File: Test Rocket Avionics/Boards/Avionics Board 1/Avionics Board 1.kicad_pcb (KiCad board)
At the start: 4 copper layers, 50 x 50 mm, 71 parts, among them J1 USB_A, J14 1S LiPo, J2 1S LiPo, J3 EXPANSION_HEADER, J4 USB_A, J5 SERVO, M2.5 CHASSIS_GND, U1 ECS-.327-12.5-17X-TR, U10 NC7WZ07, U11 LMR62014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

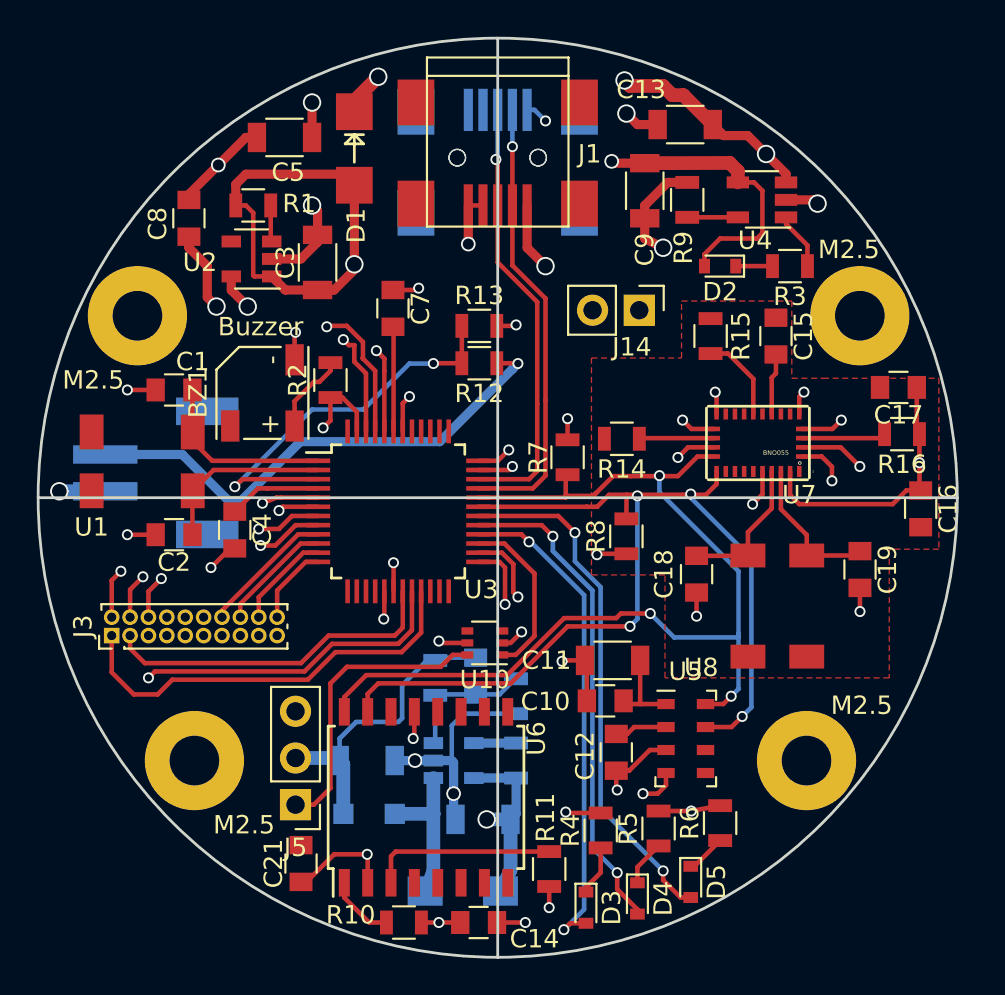
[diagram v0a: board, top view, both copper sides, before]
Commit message: Remove DS3231 and expand the J3 connector to include USB and improve pin ordering. Various bug fixes
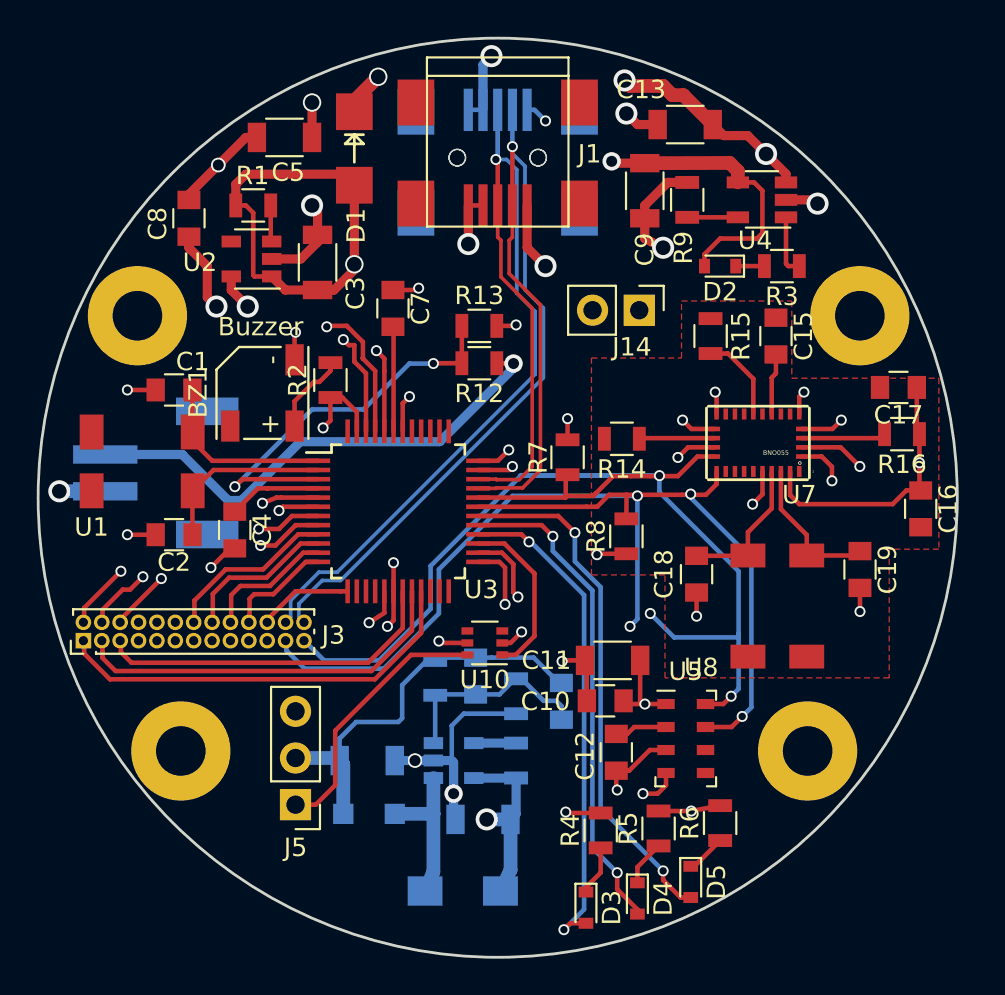
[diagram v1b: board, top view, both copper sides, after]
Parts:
- removed C21: 1u, Capacitors_SMD:C_0805
- removed M2.5: CHASSIS_GND, Mounting_Holes:MountingHole_2.7mm_M2.5_Pad
- removed R10, R11: 10k, Resistors_SMD:R_0805
- removed U6: DS3231-SO16, Housings_SOIC:SOIC-16W_7.5x10.3mm_Pitch1.27mm
- added J13: CHASSIS_GND, Mounting_Holes:MountingHole_2.7mm_M2.5_Pad, F.Cu at (28.0, 117.0)
- C22: renamed from C14; moved to B.Cu
- J3: footprint Pin_Headers:Pin_Header_Straight_2x10_Pitch1.00mm -> Pin_Headers:Pin_Header_Straight_2x13_Pitch1.00mm
- moved C22 12.8 mm to (48.7, 114.3), turned to 90 degrees
- moved G*** 1.92 mm to (44.9, 102.0)
- moved J3 1.56 mm to (22.7, 111.0)
- moved G*** 0.72 mm to (40.1, 105.0)
- moved J11 0.53 mm to (62.1, 117.0)
- moved R3 0.44 mm to (60.7, 90.6)
- renumbered M2.5 to J10, M2.5 to J11, M2.5 to J12
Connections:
- C22 pad 1: Net-(C14-Pad1) -> Net-(C22-Pad1)
- J3 pad 11: /D11 -> +3V3
- J3 pad 19: +3V3 -> /D13
- J3 pad 3: /MOSI -> /SCK
- J3 pad 5: /SCK -> /MOSI
- J3 pad 9: /D13 -> +3V3
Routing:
- net /USB_D-: track 24.6 -> 57.0 mm
- net /USB_D+: track 24.0 -> 56.1 mm
- net +3V3: track 75.0 -> 90.9 mm, vias 16 -> 14
- net /SCL: track 55.7 -> 68.8 mm
- net Net-(R11-Pad1): track 10.2 -> 0.00 mm
- net /SDA: track 55.6 -> 64.2 mm
- net GND: track 110.0 -> 117.3 mm, vias 35 -> 36
- net /D4: track 0.00 -> 5.06 mm
- net /6V_SERVO_SUPPLY: track 18.1 -> 22.1 mm
- net /D13: track 26.1 -> 22.1 mm
- net /D11: track 22.6 -> 18.7 mm
- net Net-(C22-Pad1): track 7.41 -> 11.2 mm
- net Net-(R10-Pad1): track 3.66 -> 0.00 mm
- net /A3: track 7.31 -> 9.33 mm
- net /A4: track 6.32 -> 8.33 mm
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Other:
- outline, holes or cut-outs redrawn

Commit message: Add micro SD Card, clean up ref des, power 6v boost directly from battery instead of 3.3V rail
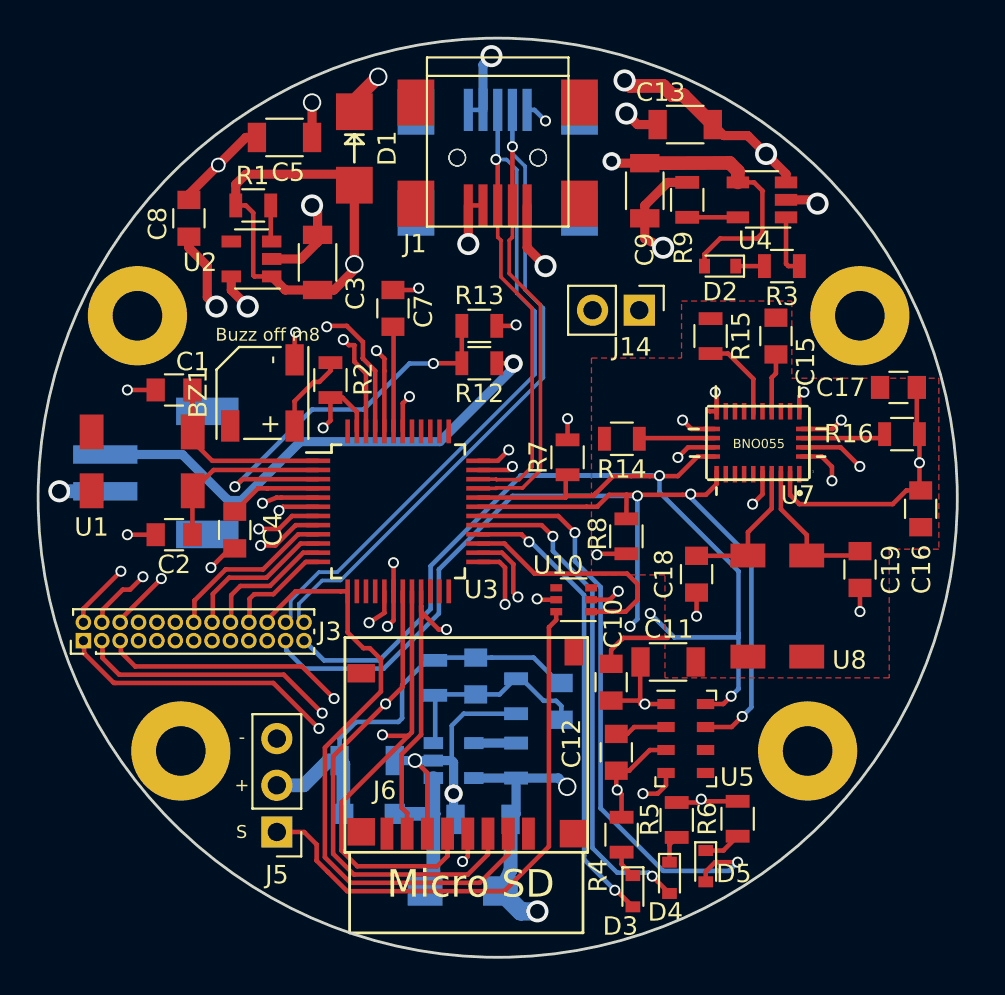
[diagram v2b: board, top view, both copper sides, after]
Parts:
- added J6: Micro_SD_Card, DannysLib:MicroSD_DM3D-SF, F.Cu at (39.2, 121.5)
- BZ1: value Buzzer -> Buzz off m8
- moved U10 5.37 mm to (49.4, 108.8)
- moved C11 3.02 mm to (54.5, 112.2), turned to 0 degrees
- moved D3 2.71 mm to (52.6, 124.6)
- moved D4 2.07 mm to (54.6, 123.9)
- moved J5 1.80 mm to (33.2, 121.4)
- moved D5 1.18 mm to (56.6, 123.3)
- moved R4 1.16 mm to (52.0, 121.6)
- moved R5 1.09 mm to (55.0, 120.8)
- moved C10 1.06 mm to (51.4, 113.3), turned to 90 degrees
- moved R6 0.98 mm to (58.3, 120.7)
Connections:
- C20 pad 1: +3V3 -> +BATT
- L1 pad 2: +3V3 -> +BATT
- R17 pad 1: +3V3 -> +BATT
- U11 pad 5: +3V3 -> +BATT
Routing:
- net +BATT: track 75.5 -> 117.5 mm, vias 4 -> 6
- net /D4: track 5.06 -> 34.1 mm
- net /MOSI: track 19.0 -> 42.6 mm, vias 0 -> 2
- net /SCK: track 21.1 -> 42.6 mm, vias 0 -> 2
- net /MISO: track 22.9 -> 40.1 mm, vias 0 -> 2
- net Net-(J5-Pad1): track 14.7 -> 30.7 mm
- net +3V3: track 90.9 -> 82.9 mm
- net GND: track 117.3 -> 122.8 mm, vias 36 -> 34
- net /D7: track 28.4 -> 32.8 mm
- net /D10: track 9.32 -> 13.2 mm
- net /D12: track 27.1 -> 25.2 mm
- net /6V_SERVO_SUPPLY: track 22.1 -> 23.9 mm
- net Net-(D4-Pad1): track 2.84 -> 1.51 mm
- net Net-(D3-Pad1): track 2.73 -> 1.53 mm
- net /D6: track 26.8 -> 27.4 mm
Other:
- board text added: "+"
- board text added: "-"
- board text added: "S"

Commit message: Add LMS303C and BMP280
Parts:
- removed C18, C19: 22p, Capacitors_SMD:C_0805
- added C14: 100n, Capacitors_SMD:C_0805, F.Cu at (60.4, 111.2)
- added C23: 100n, Capacitors_SMD:C_0805, F.Cu at (65.2, 106.1)
- added C24: 10u, Capacitors_SMD:C_1206, F.Cu at (65.2, 110.9)
- added U6: LSM303C, Housings_LGA:LGA-12_2x2mm_Pitch0.5mm, F.Cu at (61.7, 108.0)
- BZ1: value Buzz off m8 -> Buzzer
- U8: value ECS-.327-12.5-17X-TR -> BMP280; footprint DannysLib:XC1195CT-ND -> DannysLib:BMP280
- moved U8 3.30 mm to (55.6, 105.9), turned to 0 degrees
- moved L1 0.47 mm to (43.8, 124.8)
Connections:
- U8 pad 1: /BNO_OSC_OUT -> GND
- U8 pad 2: (no net) -> +3V3
- U8 pad 3: (no net) -> /SDA
- U8 pad 4: /BNO_OSC_IN -> /SCL
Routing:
- net GND: track 122.8 -> 145.0 mm, vias 34 -> 38
- net /SCL: track 68.8 -> 80.3 mm, vias 3 -> 4
- net +3V3: track 82.9 -> 94.0 mm, vias 14 -> 18
- net /BNO_OSC_IN: track 8.15 -> 0.00 mm
- net /BNO_OSC_OUT: track 7.91 -> 0.00 mm
- net /SDA: track 64.2 -> 69.6 mm, vias 4 -> 5
- net Net-(C14-Pad1): track 0.00 -> 2.46 mm

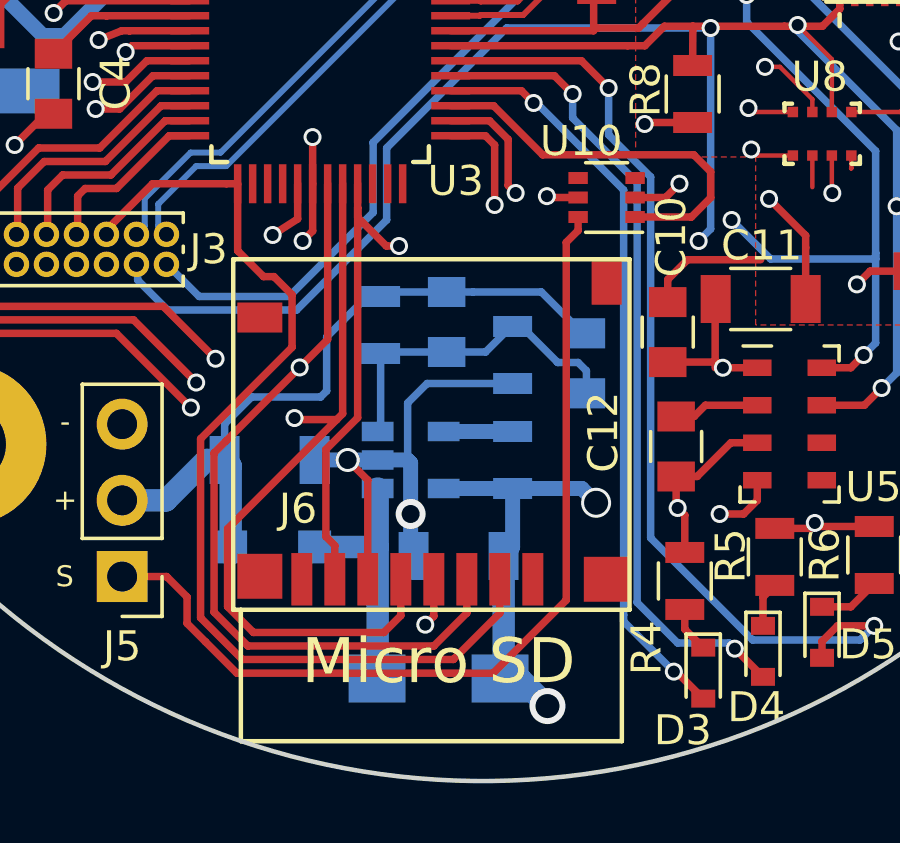
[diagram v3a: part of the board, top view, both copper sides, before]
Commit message: Create Gerbers, move SD card up for more error margin
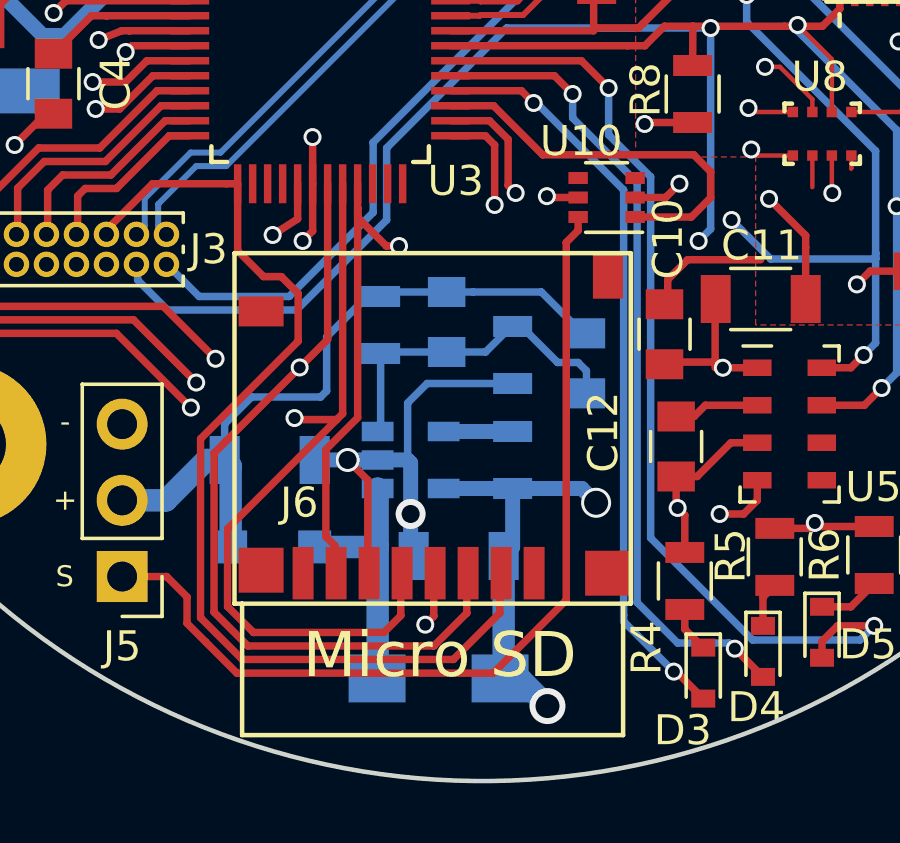
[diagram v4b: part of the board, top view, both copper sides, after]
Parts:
- moved J6 0.21 mm to (39.3, 121.3)
- moved C10 0.13 mm to (51.3, 113.3)
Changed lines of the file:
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@@
   )
   (module Capacitors_SMD:C_0805 (layer F.Cu)
-    (at 51.4096 113.2586 90)
+    (at 51.30292 113.32972 90)
     (descr "Capacitor SMD 0805, reflow soldering, AVX (see smccp.pdf)")
     (tags "capacitor 0805")
@@
   )
   (module DannysLib:MicroSD_DM3D-SF (layer F.Cu)
-    (at 39.21252 121.49836)
+    (at 39.2548 121.29516)
     (fp_text reference J6 (at -0.127 -2.3495) (layer F.SilkS)
       (effects (font (size 1 1) (thickness 0.15)))
@@
   (segment (start 32.74 109.811998) (end 34.237998 108.314) (width 0.25) (layer F.Cu) (net 36))
   (segment (start 32.74 109.922) (end 32.74 109.811998) (width 0.25) (layer F.Cu) (net 36))
-  (segment (start 45.81252 122.62336) (end 45.81252 121.49836) (width 0.25) (layer F.Cu) (net 36))
-  (segment (start 37.227637 124.171299) (end 44.26458 124.1713) (width 0.25) (layer F.Cu) (net 36))
-  (segment (start 35.837501 122.781161) (end 37.227637 124.171299) (width 0.25) (layer F.Cu) (net 36))
-  (segment (start 35.8375 116.816058) (end 35.837501 122.781161) (width 0.25) (layer F.Cu) (net 36))
-  (segment (start 37.074 108.314) (end 37.074 110.54604) (width 0.25) (layer F.Cu) (net 36))
-  (segment (start 37.074 110.54604) (end 37.93744 111.40948) (width 0.25) (layer F.Cu) (net 36))
-  (segment (start 44.26458 124.1713) (end 45.81252 122.62336) (width 0.25) (layer F.Cu) (net 36))
-  (segment (start 38.283642 111.40948) (end 38.887521 112.013359) (width 0.25) (layer F.Cu) (net 36))
-  (segment (start 37.93744 111.40948) (end 38.283642 111.40948) (width 0.25) (layer F.Cu) (net 36))
-  (segment (start 38.887521 112.013359) (end 38.887521 113.766037) (width 0.25) (layer F.Cu) (net 36))
-  (segment (start 38.887521 113.766037) (end 35.8375 116.816058) (width 0.25) (layer F.Cu) (net 36))
   (segment (start 36.14 97.772) (end 36.14 99.022) (width 0.25) (layer F.Cu) (net 37))
   (via (at 26.94 107.622) (size 0.6) (drill 0.4) (layers F.Cu B.Cu) (net 37))
@@
   (segment (start 63.12408 108.82376) (end 63.12408 112.37976) (width 0.25) (layer F.Cu) (net 2))
   (segment (start 63.4238 108.52404) (end 63.12408 108.82376) (width 0.25) (layer F.Cu) (net 2))
+  (segment (start 38.529122 111.40948) (end 37.93744 111.40948) (width 0.25) (layer F.Cu) (net 36))
+  (segment (start 39.0906 113.562958) (end 39.0906 111.970958) (width 0.25) (layer F.Cu) (net 36))
+  (segment (start 37.074 110.54604) (end 37.074 108.314) (width 0.25) (layer F.Cu) (net 36))
+  (segment (start 45.81252 121.49836) (end 45.81252 122.62336) (width 0.25) (layer F.Cu) (net 36))
+  (segment (start 45.81252 122.62336) (end 44.26458 124.1713) (width 0.25) (layer F.Cu) (net 36))
+  (segment (start 37.93744 111.40948) (end 37.074 110.54604) (width 0.25) (layer F.Cu) (net 36))
+  (segment (start 44.26458 124.1713) (end 37.227637 124.171299) (width 0.25) (layer F.Cu) (net 36))
+  (segment (start 37.227637 124.171299) (end 35.837501 122.781161) (width 0.25) (layer F.Cu) (net 36))
+  (segment (start 35.837501 122.781161) (end 35.8375 116.816058) (width 0.25) (layer F.Cu) (net 36))
+  (segment (start 39.0906 111.970958) (end 38.529122 111.40948) (width 0.25) (layer F.Cu) (net 36))
+  (segment (start 35.8375 116.816058) (end 39.0906 113.562958) (width 0.25) (layer F.Cu) (net 36))
   (zone (net 2) (net_name GND) (layer Ground_Plane) (hatch edge 0.508)
     (connect_pads (clearance 0.508))
